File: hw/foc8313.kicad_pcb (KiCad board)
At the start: 4 copper layers, 35 x 35 mm, 70 parts, among them J1 Tag Connect, J2 CAN, J3 CAN, P1 USB_C_Plug, U1 DRV8313PWP, U10 XC6206P332MR, U2 STM32F103CBTx, U3 AS5047D, U4 INA240A2D, U5 INA240A2D, U6 TJA1044GT/3Z, U7 LMR36015SFBRNXR, U8 INA240A2D, X1 X322516MLB4SI

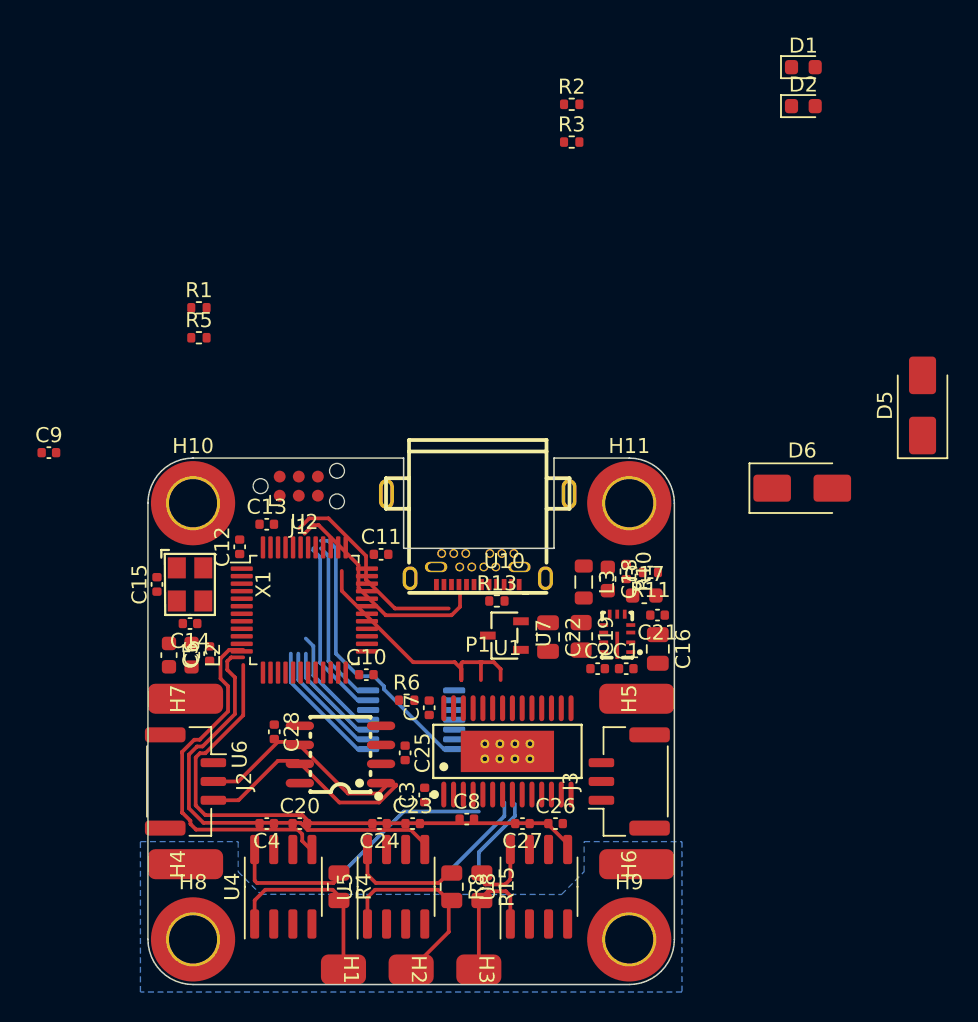
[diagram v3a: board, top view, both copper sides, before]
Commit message: [Hw] Decent current sense layout
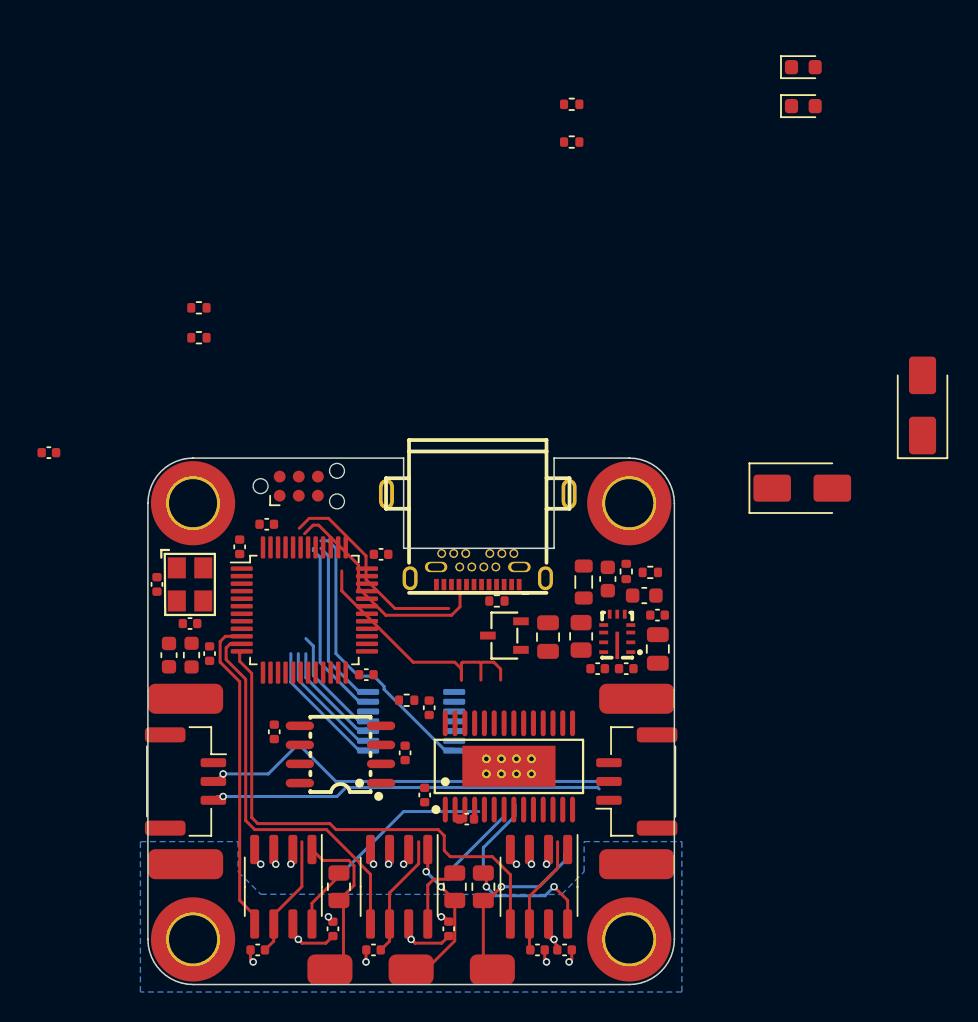
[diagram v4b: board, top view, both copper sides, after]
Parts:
- moved C20 8.85 mm to (129.8, 115.2), turned to 180 degrees
- moved C27 8.85 mm to (150.2, 115.2), turned to 0 degrees
- moved C23 8.79 mm to (137.5, 115.2), turned to 180 degrees
- moved C26 8.49 mm to (148.4, 115.2)
- moved C24 8.38 mm to (142.5, 113.8), turned to 90 degrees
- moved C4 8.27 mm to (134.8, 113.8), turned to 90 degrees
- moved U1 1.00 mm to (146.5, 103.0)
- moved H1 0.90 mm to (134.6, 116.5)
- moved H3 0.90 mm to (145.4, 116.5)
- moved J3 0.50 mm to (155.0, 104.0)
- moved R8 0.20 mm to (142.9, 111.0)
- moved U5 0.20 mm to (139.2, 111.0), turned to -90 degrees
- moved R15 0.10 mm to (144.8, 111.0)
- moved U3 0.10 mm to (140.0, 100.0)
- turned U4 to -90 degrees
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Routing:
- net +3.3V: track 0.00 -> 24.5 mm
- net GND: track 0.00 -> 14.1 mm, vias 0 -> 15
- net /CAN.L: track 14.2 -> 27.7 mm, vias 0 -> 1
- net /CAN.H: track 14.9 -> 26.0 mm, vias 0 -> 1
- net +3.3VA: track 0.00 -> 9.91 mm, vias 0 -> 3
- net /PHA: track 8.31 -> 4.13 mm
- net /PHC: track 10.7 -> 14.2 mm, vias 0 -> 2
- net /ISENSE_B: track 29.7 -> 26.3 mm
- net /OUTC: track 8.94 -> 11.9 mm, vias 0 -> 1
- net /PHB: track 7.67 -> 4.71 mm
- net /ISENSE_C: track 37.0 -> 34.1 mm
- net /ISENSE_A: track 23.8 -> 21.3 mm
- net /OUTB: track 13.3 -> 11.0 mm, vias 0 -> 2
- net /OUTA: track 12.6 -> 10.7 mm
- added copper zone on In1.Cu, net +3.3VA
- removed copper zone on In1.Cu, net GNDA

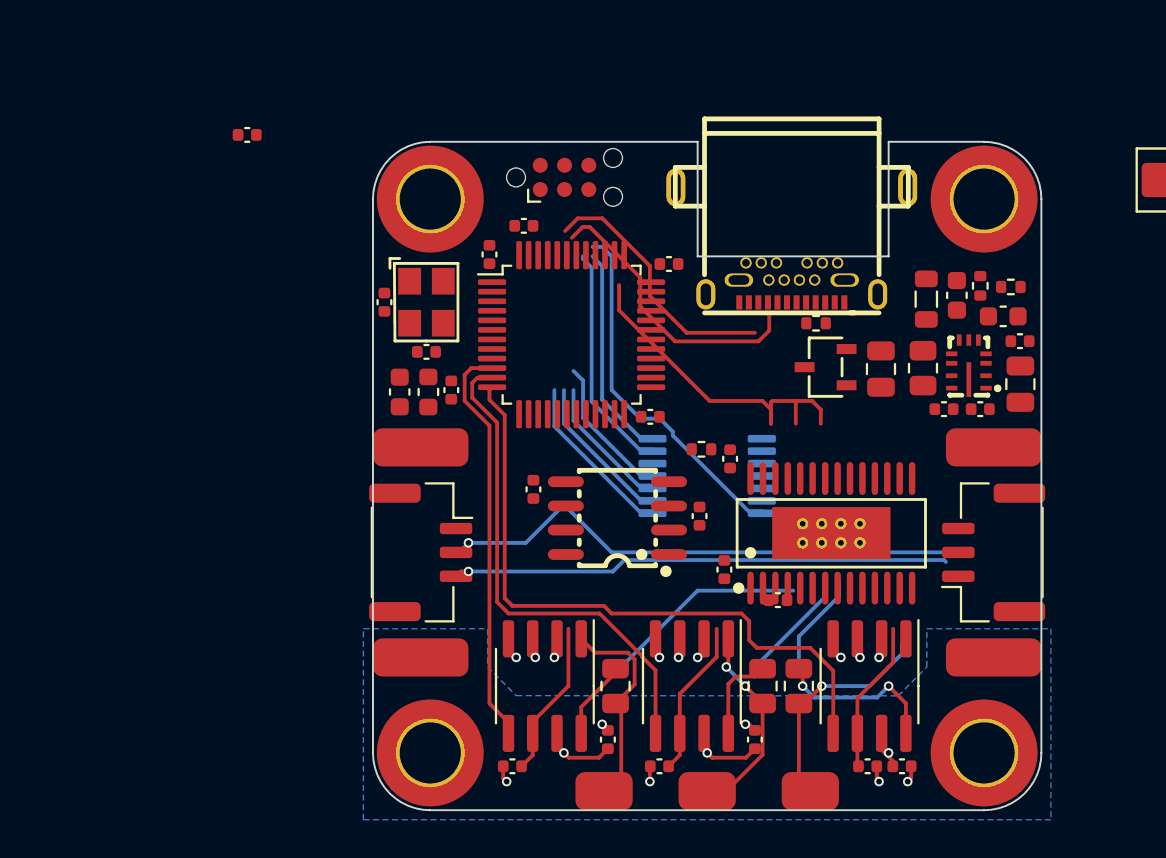
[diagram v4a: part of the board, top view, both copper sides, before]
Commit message: [Hw] compact discrete 4 wire iso can, approx drv routing, eeprom
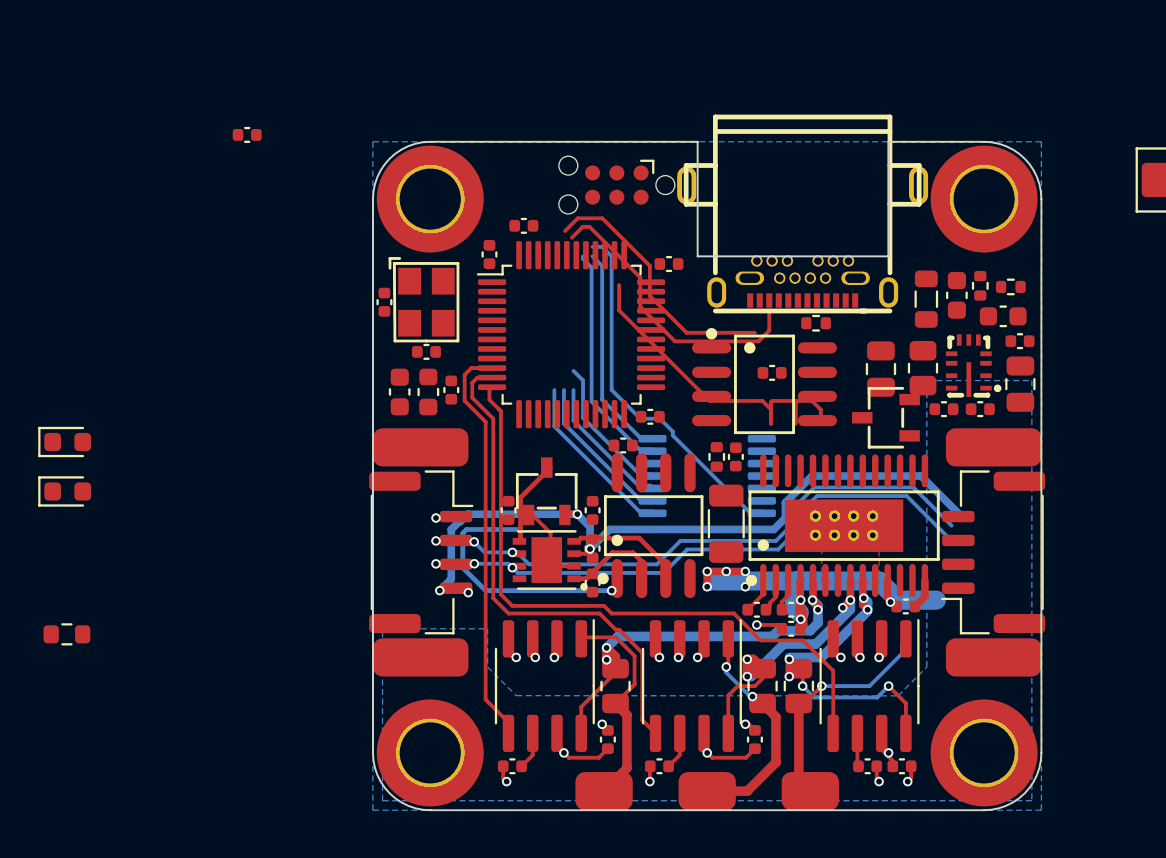
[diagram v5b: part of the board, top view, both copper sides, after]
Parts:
- removed C28: 100n, Capacitor_SMD:C_0402_1005Metric
- added C29: 100n, Capacitor_SMD:C_0402_1005Metric, F.Cu at (150.4, 106.8)
- added C30: 100n, Capacitor_SMD:C_0402_1005Metric, F.Cu at (144.4, 108.0)
- added C31: 10u, Capacitor_SMD:C_1206_3216Metric, F.Cu at (141.0, 102.5)
- added C32: 100n, Capacitor_SMD:C_0402_1005Metric, F.Cu at (134.0, 105.6)
- added C33: 100n, Capacitor_SMD:C_0402_1005Metric, F.Cu at (135.6, 98.4)
- added C34: 100n, Capacitor_SMD:C_0402_1005Metric, F.Cu at (129.6, 101.8)
- added C35: 100n, Capacitor_SMD:C_0402_1005Metric, F.Cu at (134.0, 103.8)
- added C38: 100n, Capacitor_SMD:C_0402_1005Metric, F.Cu at (134.0, 101.8)
- added D4: 5V, Diode_SMD:D_0603_1608Metric, F.Cu at (106.5, 98.2)
- added D8: BLUE, LED_SMD:LED_0603_1608Metric, F.Cu at (106.5, 100.8)
- added R9: 1k5, Resistor_SMD:R_0603_1608Metric, F.Cu at (106.5, 108.3)
- added U11: TJA1051TK/3,118, easyeda:HVSON-8_L3.0-W3.0-P0.65-BL-EP, F.Cu at (131.6, 104.4)
- added U12: ADUM1201ARZ-RL7, easyeda:SOIC-8_L4.9-W3.9-P1.27-LS6.0-BL, F.Cu at (137.2, 102.6)
- added U13: XC6206P332MR, easyeda:SOT-23-3_L2.9-W1.6-P1.90-LS2.8-BR, F.Cu at (131.6, 100.8)
- J2, J3: footprint Connector_JST:JST_GH_SM03B-GHS-TB_1x03-1MP_P1.25mm_Horizontal -> Connector_JST:JST_GH_SM04B-GHS-TB_1x04-1MP_P1.25mm_Horizontal
- U10: footprint easyeda:SOT-23-3_L3.0-W1.7-P0.95-LS2.9-BR -> easyeda:SOT-23-3_L2.9-W1.6-P1.90-LS2.8-BR
- U6: value TJA1044GT/3Z -> AT24C256C-SSHL-T; footprint easyeda:SO-8_L4.9-W3.9-P1.27-LS5.9-BL -> easyeda:SOIC-8_L4.9-W3.9-P1.27-LS6.0-BL
- moved U6 10.4 mm to (143.0, 95.2), turned to -90 degrees
- moved C25 8.41 mm to (143.4, 94.6), turned to 0 degrees
- moved U10 4.12 mm to (149.4, 97.0)
- moved J1 2.77 mm to (135.3, 84.8), turned to 180 degrees
- moved C3 2.70 mm to (142.6, 107.0), turned to 0 degrees
- moved R6 0.89 mm to (140.5, 99.0), turned to 90 degrees
- moved C8 0.86 mm to (144.4, 107.0)
- moved U1 0.78 mm to (147.2, 102.6)
- moved P1 0.58 mm to (145.0, 87.8)
- moved C7 0.32 mm to (141.5, 99.0)
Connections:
- C25 pad 1: +5V -> GND
- C25 pad 2: GND -> Net-(U6-VCC)
- U10 pad 2: +3.3V -> +5V
- U10 pad 3: +5V -> +3.3V
- U6 pad 1: /CAN.TX -> GND
- U6 pad 3: +5V -> GND
- U6 pad 4: /CAN.RX -> GND
- U6 pad 5: +3.3V -> /I2C.SDA
- U6 pad 6: /CAN.L -> /I2C.SCL
- U6 pad 7: /CAN.H -> GND
- U6 pad 8: unconnected-(U6-STB-Pad8) -> Net-(U6-VCC)
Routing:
- net /CAN.V+: track 0.00 -> 35.9 mm, vias 0 -> 4
- net VCC: track 0.00 -> 22.9 mm, vias 0 -> 8
- net +3.3V: track 24.5 -> 5.77 mm
- net Net-(U11-VIO): track 0.00 -> 17.8 mm, vias 0 -> 1
- net (no net): track 16.8 -> 0.00 mm
- net /PHA: track 4.13 -> 20.7 mm, vias 0 -> 4
- net /PHB: track 4.71 -> 15.5 mm, vias 0 -> 4
- net Net-(U11-RXD): track 0.00 -> 5.98 mm
- net Net-(U11-TXD): track 0.00 -> 4.99 mm
- net /CAN.V-: track 0.00 -> 4.32 mm, vias 0 -> 1
- net GND: track 14.1 -> 17.0 mm, vias 15 -> 16
- net /CAN.H: track 26.0 -> 28.9 mm, vias 1 -> 3
- net /PHC: track 14.2 -> 16.8 mm, vias 2 -> 6
- net Net-(U1-CPL): track 0.00 -> 1.87 mm
- net Net-(U1-VCP): track 0.00 -> 1.68 mm
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- added copper zone on In2.Cu, net /CAN.V-
- added copper zone on B.Cu, net GND
- added copper zone on F.Cu, net GND

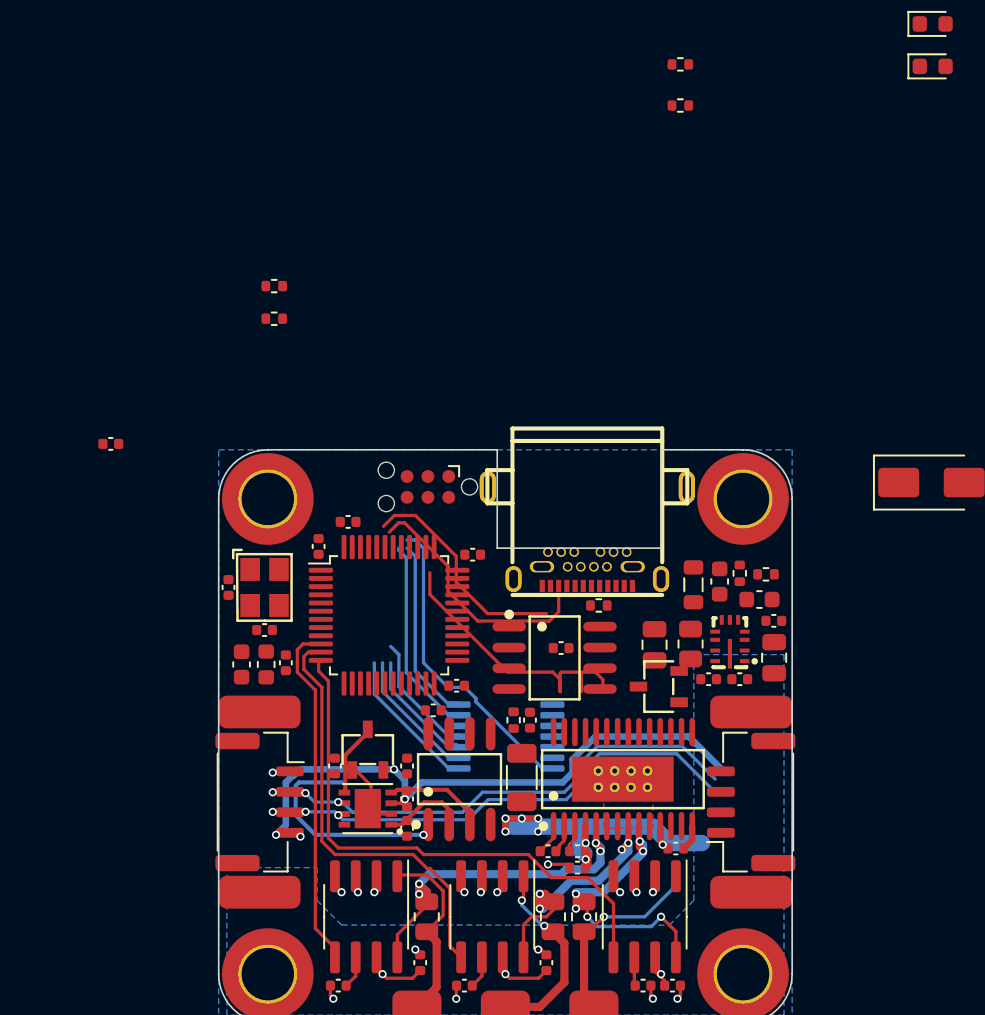
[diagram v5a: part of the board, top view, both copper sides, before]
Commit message: [Hw] Squeezing in push button and aux 8 pin connector
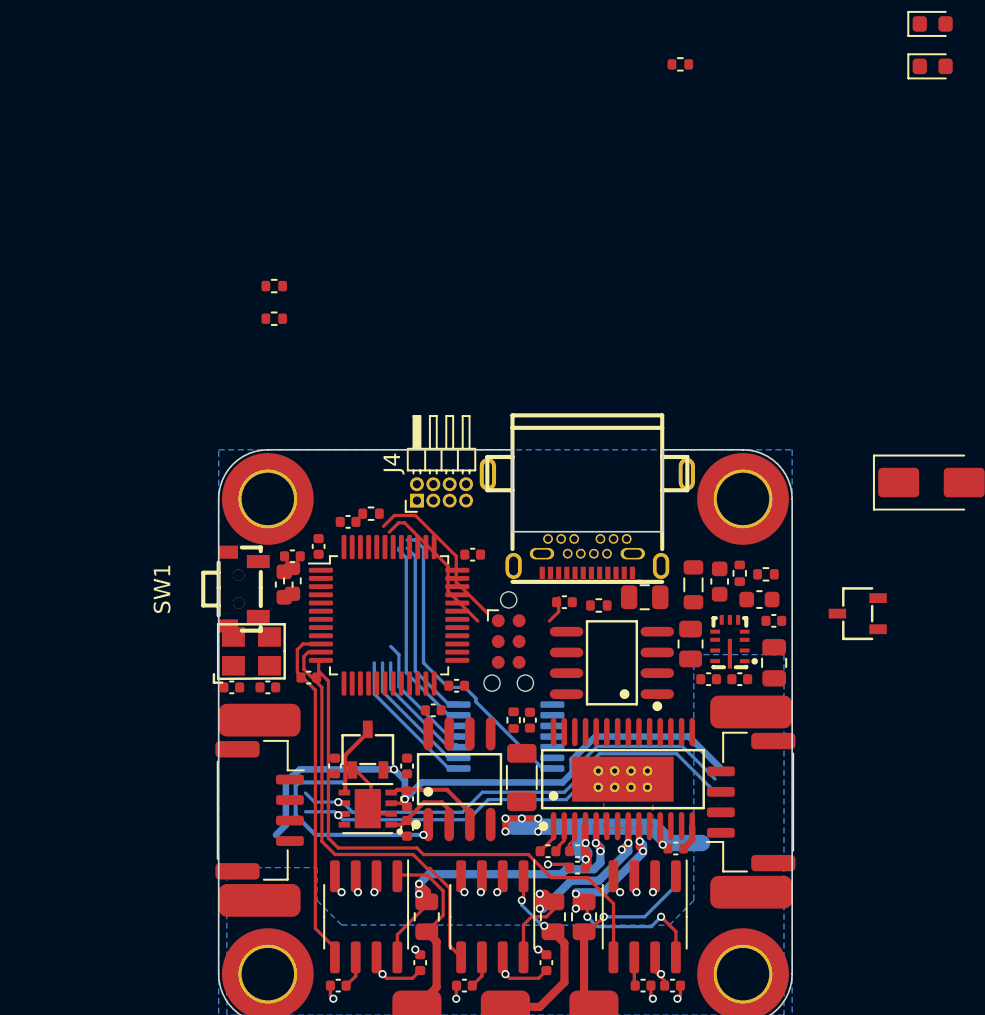
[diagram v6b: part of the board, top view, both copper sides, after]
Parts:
- added J4: Aux, Connector_PinHeader_1.00mm:PinHeader_2x04_P1.00mm_Horizontal, F.Cu at (134.6, 85.6)
- added SW1: SW_SPST, easyeda:SW-SMD_L4.7-W3.5-P3.35-EH, F.Cu at (124.0, 91.0)
- moved R3 31.3 mm to (131.8, 86.4)
- moved C9 13.0 mm to (127.0, 89.0)
- moved U10 12.9 mm to (161.5, 92.5)
- moved J1 10.6 mm to (140.2, 94.2), turned to -90 degrees
- moved C15 6.56 mm to (125.5, 97.0), turned to 180 degrees
- moved C5 5.52 mm to (126.5, 90.7), turned to 90 degrees
- moved L2 5.35 mm to (127.0, 90.5)
- moved C14 4.03 mm to (123.3, 97.0)
- moved X1 3.98 mm to (124.5, 94.8), turned to 0 degrees
- moved U6 3.51 mm to (146.5, 95.5), turned to 90 degrees
- moved C22 2.96 mm to (148.5, 91.5), turned to 180 degrees
- moved C25 2.81 mm to (143.6, 91.8)
- moved C6 1.66 mm to (128.0, 96.4), turned to 180 degrees
- moved P1 0.80 mm to (145.0, 87.0)
- moved H4 0.50 mm to (125.0, 110.0)
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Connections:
- C1 pad 2: GND -> +3V3
- C10 pad 2: GND -> +3V3
- C11 pad 2: GND -> +3V3
- C12 pad 2: GND -> +3V3
- C13 pad 2: GND -> +3V3
- C14 pad 2: GND -> +3V3
- C15 pad 1: GND -> +3V3
- C16 pad 2: GND -> +3V3
- C17 pad 2: GND -> +3V3
- C19 pad 2: GND -> +3V3
- C2 pad 2: GND -> +3V3
- C20 pad 2: GND -> +3V3
- C22 pad 2: GND -> +3V3
- C23 pad 2: GND -> +3V3
- C24 pad 2: GND -> +3V3
- C25 pad 1: GND -> +3V3
- C26 pad 2: GND -> +3V3
- C27 pad 2: GND -> +3V3
- C29 pad 2: GND -> +3V3
- C30 pad 2: GND -> +3V3
- C31 pad 2: GND -> +3V3
- C33 pad 2: GND -> +3V3
- C4 pad 2: GND -> +3V3
- C5 pad 2: GND -> +3V3
- C6 pad 2: GND -> +3V3
- C7 pad 2: GND -> +3V3
- C9 pad 2: GND -> +3V3
- H5 pad 1: GND -> +3V3
- H7 pad 1: GND -> +3V3
- J1 pad 5: GND -> +3V3
- P1 pad A1: GND -> +3V3
- P1 pad A12: GND -> +3V3
- P1 pad B1: GND -> +3V3
- P1 pad B12: GND -> +3V3
- R11 pad 2: GND -> +3V3
- R13 pad 2: GND -> +3V3
- R3 pad 1: GND -> +3V3
- R5 pad 2: GND -> +3V3
- R9 pad 2: GND -> +3V3
- U1 pad 10: GND -> +3V3
- U1 pad 14: GND -> +3V3
- U1 pad 20: GND -> +3V3
- U1 pad 28: GND -> +3V3
- U1 pad 29: GND -> +3V3
- U1 pad 6: GND -> +3V3
- U1 pad 7: GND -> +3V3
- U10 pad 1: GND -> +3V3
- U12 pad 5: GND -> +3V3
- U2 pad 23: GND -> +3V3
- U2 pad 35: GND -> +3V3
- U2 pad 47: GND -> +3V3
- U3 pad 13: GND -> +3V3
- U3 pad 5: GND -> +3V3
- U4 pad 2: GND -> +3V3
- U4 pad 3: GND -> +3V3
- U4 pad 4: GND -> +3V3
- U5 pad 2: GND -> +3V3
- U5 pad 3: GND -> +3V3
- U5 pad 4: GND -> +3V3
- U6 pad 1: GND -> +3V3
- U6 pad 2: GND -> +3V3
- U6 pad 3: GND -> +3V3
- U6 pad 4: GND -> +3V3
- U6 pad 7: GND -> +3V3
- U7 pad 1: GND -> +3V3
- U7 pad 11: GND -> +3V3
- U7 pad 6: GND -> +3V3
- U8 pad 2: GND -> +3V3
- U8 pad 3: GND -> +3V3
- U8 pad 4: GND -> +3V3
- X1 pad 2: GND -> +3V3
- X1 pad 4: GND -> +3V3
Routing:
- net +3V3: track 0.00 -> 18.7 mm, vias 0 -> 16
- net /DRV_EN: track 18.0 -> 0.00 mm
- net GND: track 17.0 -> 0.00 mm, vias 16 -> 0
- net /USB_DM: track 15.0 -> 9.01 mm
- net /USB_DP: track 13.6 -> 10.0 mm
- net /CAN.V-: vias 1 -> 0
- net /CAN.V+: vias 4 -> 2
- net /CAN.L: vias 3 -> 1
- net /CAN.H: vias 3 -> 1
- added copper zone on B.Cu, net +3V3
- added copper zone on F.Cu, net +3V3
- added copper zone on In1.Cu, net +3V3
- added copper zone on In2.Cu, net +3V3
- removed copper zone on B.Cu, net GND
- removed copper zone on F.Cu, net GND
- removed copper zone on In1.Cu, net GND
- removed copper zone on In2.Cu, net GND
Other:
- outline, holes or cut-outs redrawn
